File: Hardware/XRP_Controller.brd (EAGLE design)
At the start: 63.5 x 54 mm, 212 parts, among them J1 POWER_JACKPOWER_JACK_SLOT, J12 Vertical Qwiic Connector, J13 Vertical Qwiic Connector, J14 Vertical Qwiic Connector, J3 JST_6_PIN_VERTICAL, J4 JST_6_PIN_VERTICAL, J5 JST_6_PIN_VERTICAL, J6 JST_6_PIN_VERTICAL, J9 Vertical Qwiic Connector, Q3 20V/4.2A/52mΩ/1.4W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

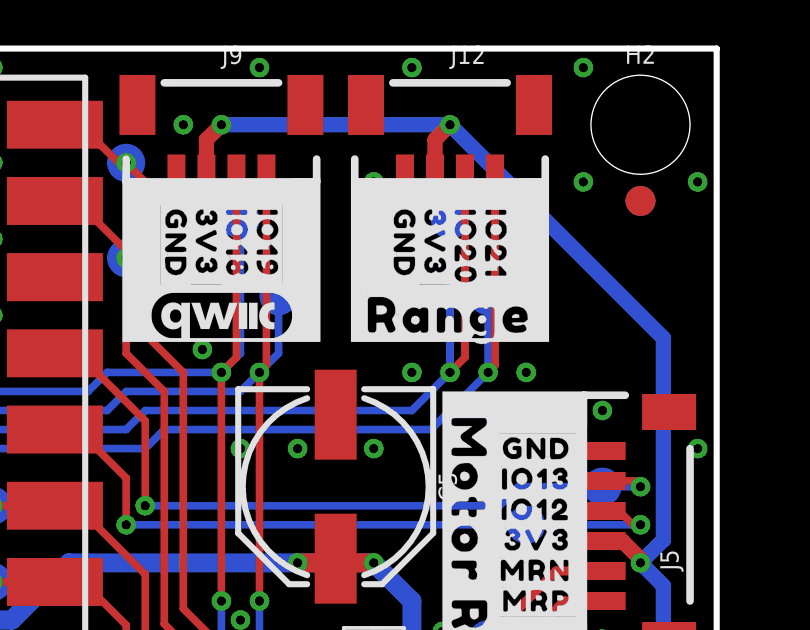
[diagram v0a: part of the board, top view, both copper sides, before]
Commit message: Fix "Range" silk
Modify the Buzzard footprint to have a lower bottom edge
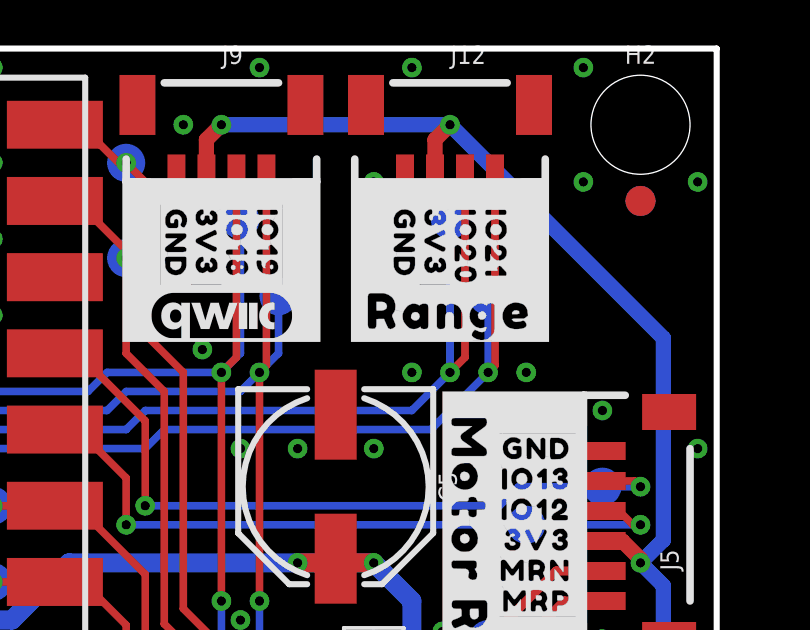
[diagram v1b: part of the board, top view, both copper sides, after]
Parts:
- removed U$73: (no value), output:#RANGE#0
- added U$69: (no value), output:#RANGE#0
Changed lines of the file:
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@@
 <rectangle x1="51.308" y1="44.323" x2="51.435" y2="45.847" layer="21"/>
 <rectangle x1="57.785" y1="44.323" x2="57.912" y2="45.847" layer="21"/>
-<rectangle x1="51.308" y1="44.196" x2="57.912" y2="44.323" layer="21"/>
+<rectangle x1="51.308" y1="44.196" x2="55.372" y2="44.323" layer="21"/>
 <rectangle x1="10.922" y1="45.847" x2="12.192" y2="49.657" layer="21"/>
 <rectangle x1="5.588" y1="45.847" x2="6.858" y2="49.657" layer="21"/>
@@
 <rectangle x1="39.243" y1="31.623" x2="39.624" y2="31.877" layer="41"/>
 <rectangle x1="17.653" y1="16.129" x2="17.907" y2="16.256" layer="41"/>
+<rectangle x1="56.007" y1="44.196" x2="57.912" y2="44.323" layer="21"/>
+<rectangle x1="55.372" y1="44.196" x2="56.007" y2="44.2468" layer="21"/>
 </plain>
 <attributes>
@@
 <attribute name="VALUE" x="17.315" y="19.525" size="1.27" layer="27"/>
 </element>
-<element name="U$73" library="output" package="#RANGE#0" value="" x="54.61" y="45.085" smashed="yes"/>
 <element name="U$74" library="output" package="#LINE#0" value="" x="8.89" y="45.085" smashed="yes"/>
 <element name="U$10" library="output" package="#MOTOR_L#0" value="" x="8.255" y="38.1" smashed="yes" rot="R90"/>
@@
 <element name="TP39" library="SparkFun-Connectors" package="PAD.03X.05" value="TEST-POINT3X5" x="50.8" y="22.86" smashed="yes" rot="MR0"/>
 <element name="TP38" library="SparkFun-Connectors" package="PAD.03X.05" value="TEST-POINT3X5" x="45.085" y="19.685" smashed="yes" rot="MR0"/>
+<element name="U$69" library="output" package="#RANGE#0" value="" x="54.61" y="45.212" smashed="yes"/>
 </elements>
 <signals>

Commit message: Connect SCX pin of IMU to GND
Datasheet says to do this, whoops!
Pins 10-12 have internal pullups, can leave unconnected
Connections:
- net GND: now also U4.3
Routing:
- net GND: track 7.35 -> 8.08 mm
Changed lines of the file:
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@@
 <via x="7.239" y="26.289" extent="1-16" drill="0.3048"/>
 <wire x1="45.815" y1="23.11" x2="45.3106625" y2="23.11" width="0.254" layer="1"/>
-<wire x1="45.085" y1="22.8843375" x2="45.085" y2="22.225" width="0.254" layer="1"/>
+<wire x1="45.085" y1="22.8843375" x2="45.085" y2="22.606" width="0.254" layer="1"/>
+<wire x1="45.085" y1="22.606" x2="45.085" y2="22.225" width="0.254" layer="1"/>
 <wire x1="45.3106625" y1="23.11" x2="45.085" y2="22.8843375" width="0.254" layer="1"/>
 <contactref element="J8" pad="3"/>
@@
 <contactref element="U1" pad="28"/>
 <via x="50.8" y="21.336" extent="1-16" drill="0.3048"/>
+<contactref element="U4" pad="3"/>
+<wire x1="45.815" y1="22.61" x2="45.089" y2="22.61" width="0.254" layer="1"/>
+<wire x1="45.089" y1="22.61" x2="45.085" y2="22.606" width="0.254" layer="1"/>
 </signal>
 <signal name="3.3V">

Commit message: Put all XRP specific parts into a single library
Helps ensure PROD_ID values are correct for this project
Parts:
- U1: value RPI_PICO_W -> RPI_PICO_W_XRP; device RPI_PICO_W:RPI_PICO_W -> XRP_COMPONENTS:RPI_PICO_W
- U4: value LSM6DS0 -> LSM6DS0X; device SparkFun-Sensors:LGA14L -> XRP_COMPONENTS:LGA14L
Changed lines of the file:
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@@
 <attribute name="VALUE" x="47.006" y="51.40866875" size="0.6096" layer="27"/>
 </element>
-<element name="U4" library="SparkFun-Sensors" package="LGA14L" value="LSM6DS0" x="46.99" y="22.86" smashed="yes">
+<element name="U4" library="XRP_COMPONENTS" package="LGA14L" value="LSM6DS0X" x="46.99" y="22.86" smashed="yes">
 <attribute name="NAME" x="45.633" y="24.632" size="0.6096" layer="27" font="vector" ratio="20"/>
-<attribute name="PROD_ID" value="IC-15837" x="46.99" y="22.86" size="1.778" layer="27" font="vector" ratio="15" display="off"/>
-<attribute name="VALUE" x="45.379" y="20.469" size="0.6096" layer="27" font="vector" ratio="20"/>
+<attribute name="PROD_ID" value="IC-18009" x="46.99" y="22.86" size="1.778" layer="27" font="vector" ratio="15" display="off"/>
+<attribute name="VALUE" value="LSM6DS0X" x="45.379" y="20.469" size="0.6096" layer="27" font="vector" ratio="20"/>
 </element>
 <element name="U5" library="SparkFun-IC-Special-Function" package="WSON-12" value="DRV8835" x="11.43" y="33.02" smashed="yes" rot="R270">
@@
 <attribute name="VALUE" x="9.144" y="16.129" size="0.6096" layer="27" font="vector" ratio="20" rot="R90" align="top-center"/>
 </element>
-<element name="U1" library="RPI_PICO_W" package="RPI_PICO_W" value="RPI_PICO_W" x="31.75" y="27.305" smashed="yes" rot="R180">
+<element name="U1" library="XRP_COMPONENTS" package="RPI_PICO_W" value="RPI_PICO_W_XRP" x="31.75" y="27.305" smashed="yes" rot="R180">
 <attribute name="NAME" x="31.75" y="-0.195" size="0.6096" layer="25" font="vector" ratio="20" rot="R180" align="center"/>
-<attribute name="PROD_ID" value="COMP-16830" x="31.75" y="27.305" size="1.778" layer="27" font="vector" ratio="15" rot="R180" display="off"/>
+<attribute name="PROD_ID" value="COMP-18042" x="31.75" y="27.305" size="1.778" layer="27" font="vector" ratio="15" rot="R180" display="off"/>
 <attribute name="VALUE" x="31.75" y="54.805" size="0.6096" layer="27" font="vector" ratio="20" rot="R180" align="center"/>
 </element>

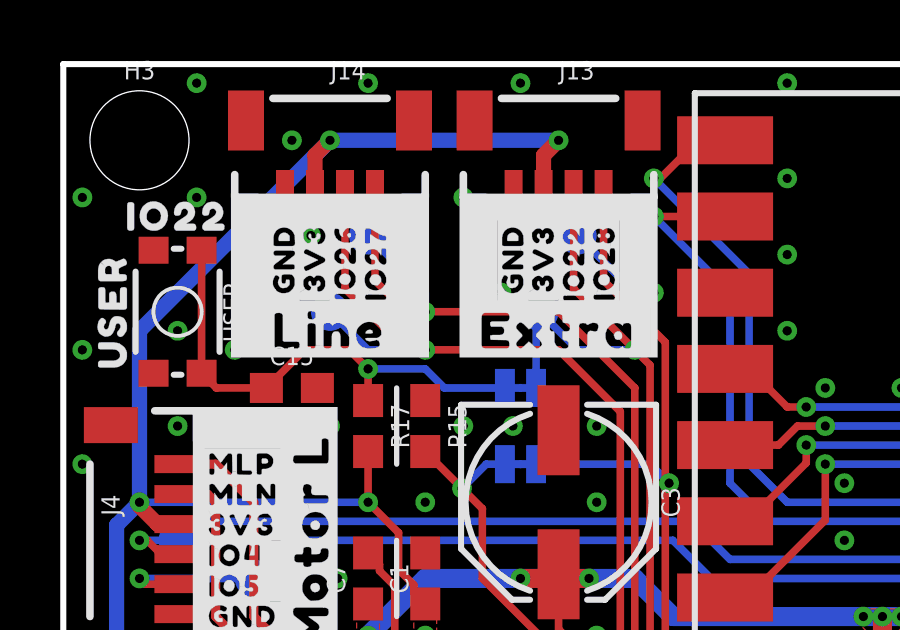
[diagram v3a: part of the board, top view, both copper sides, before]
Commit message: Nudge vias to clean up silk text
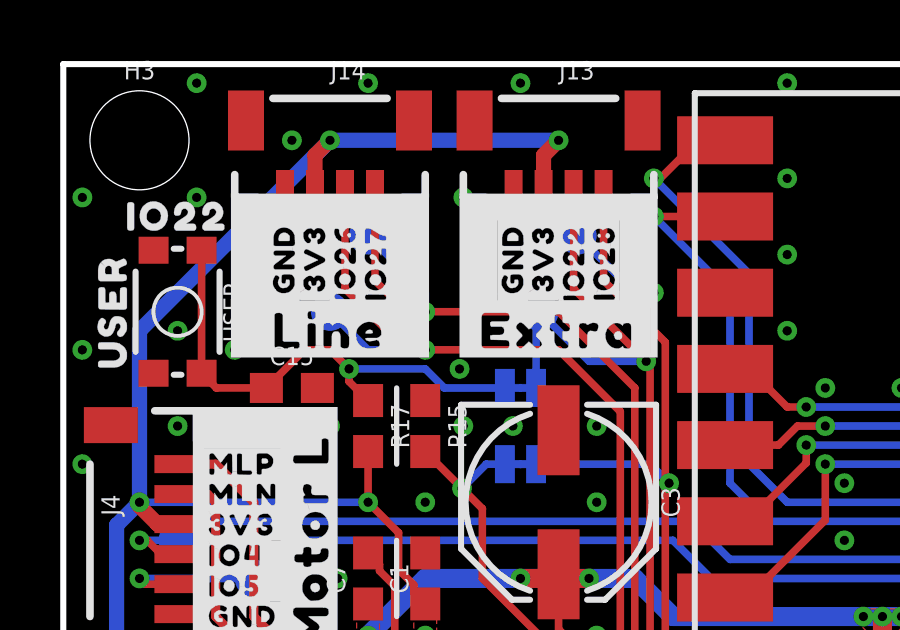
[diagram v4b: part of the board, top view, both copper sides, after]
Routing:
- net RP_IO22/USER_BTN: track 28.2 -> 28.7 mm
- net GND: vias 202 -> 203
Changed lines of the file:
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@@
 <via x="38.735" y="8.89" extent="1-16" drill="0.3048"/>
 <via x="59.69" y="12.7" extent="1-16" drill="0.3048"/>
-<via x="14.605" y="46.355" extent="1-16" drill="0.3048"/>
-<via x="8.255" y="48.26" extent="1-16" drill="0.3048"/>
+<via x="13.97" y="46.355" extent="1-16" drill="0.3048"/>
+<via x="6.35" y="47.625" extent="1-16" drill="0.3048"/>
 <contactref element="R15" pad="1"/>
 <via x="13.335" y="41.91" extent="1-16" drill="0.3048"/>
@@
 <wire x1="45.815" y1="22.61" x2="45.089" y2="22.61" width="0.254" layer="1"/>
 <wire x1="45.089" y1="22.61" x2="45.085" y2="22.606" width="0.254" layer="1"/>
+<via x="13.208" y="43.815" extent="1-16" drill="0.3048"/>
 </signal>
 <signal name="3.3V">
@@
 <wire x1="19.558" y1="31.496" x2="19.558" y2="43.942" width="0.254" layer="1"/>
 <contactref element="J13" pad="3"/>
-<wire x1="19.558" y1="43.942" x2="19.05" y2="44.45" width="0.254" layer="1"/>
+<wire x1="19.558" y1="43.942" x2="19.431" y2="44.069" width="0.254" layer="1"/>
 <contactref element="TP21" pad="1"/>
-<via x="19.05" y="44.45" extent="1-16" drill="0.3048"/>
-<wire x1="19.05" y1="44.45" x2="17.145" y2="44.45" width="0.254" layer="16"/>
-<wire x1="17.145" y1="44.45" x2="15.875" y2="45.72" width="0.254" layer="16"/>
+<via x="19.431" y="44.069" extent="1-16" drill="0.3048"/>
+<wire x1="19.431" y1="44.069" x2="17.526" y2="44.069" width="0.254" layer="16"/>
+<wire x1="17.526" y1="44.069" x2="15.875" y2="45.72" width="0.254" layer="16"/>
 <contactref element="USER_BTN" pad="2"/>
 <wire x1="15.7607" y1="43.18" x2="15.7607" y2="45.6057" width="0.254" layer="16"/>
 <wire x1="15.7607" y1="45.6057" x2="15.875" y2="45.72" width="0.254" layer="16"/>
 <wire x1="17.01" y1="49.67" x2="17.01" y2="46.49" width="0.254" layer="1"/>
-<wire x1="17.01" y1="46.49" x2="19.05" y2="44.45" width="0.254" layer="1"/>
+<wire x1="17.01" y1="46.49" x2="19.431" y2="44.069" width="0.254" layer="1"/>
 <contactref element="U1" pad="29"/>
 </signal>
@@
 <wire x1="4.61" y1="43.67" x2="5.1" y2="43.18" width="0.254" layer="1"/>
 <wire x1="5.1" y1="43.18" x2="6.77" y2="43.18" width="0.254" layer="1"/>
-<wire x1="10.16" y1="42.76" x2="10.16" y2="43.815" width="0.254" layer="1"/>
-<wire x1="10.16" y1="43.815" x2="9.525" y2="44.45" width="0.254" layer="1"/>
-<wire x1="9.525" y1="44.45" x2="8.04" y2="44.45" width="0.254" layer="1"/>
+<wire x1="10.16" y1="42.76" x2="9.525" y2="43.395" width="0.254" layer="1"/>
+<wire x1="9.525" y1="43.815" x2="9.525" y2="43.395" width="0.254" layer="1"/>
+<wire x1="9.525" y1="43.815" x2="8.89" y2="44.45" width="0.254" layer="1"/>
+<wire x1="8.89" y1="44.45" x2="8.04" y2="44.45" width="0.254" layer="1"/>
 <wire x1="8.04" y1="44.45" x2="6.77" y2="43.18" width="0.254" layer="1"/>
-<via x="10.16" y="43.815" extent="1-16" drill="0.3048"/>
-<wire x1="10.16" y1="43.815" x2="12.065" y2="43.815" width="0.254" layer="16"/>
+<via x="9.525" y="43.815" extent="1-16" drill="0.3048"/>
+<wire x1="9.525" y1="43.815" x2="12.065" y2="43.815" width="0.254" layer="16"/>
 <wire x1="12.065" y1="43.815" x2="12.7" y2="43.18" width="0.254" layer="16"/>
 <wire x1="12.7" y1="43.18" x2="14.7193" y2="43.18" width="0.254" layer="16"/>

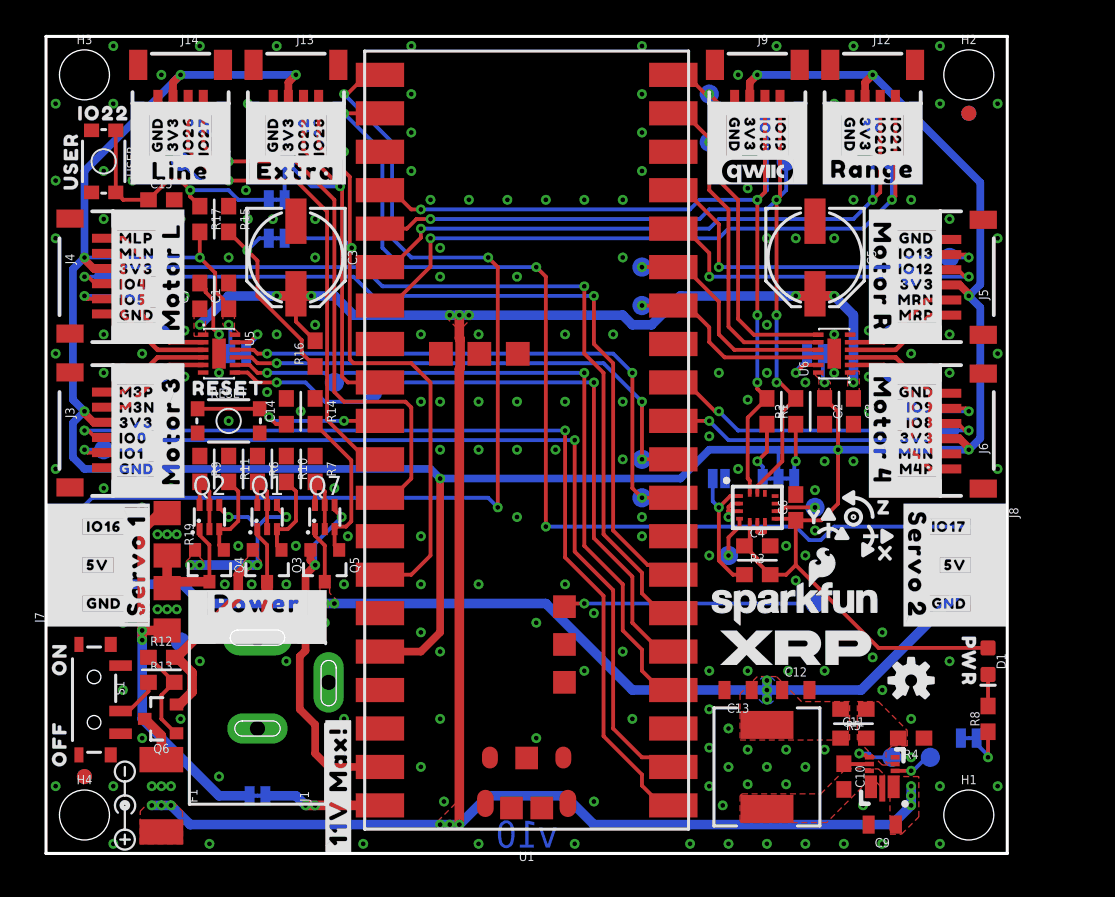
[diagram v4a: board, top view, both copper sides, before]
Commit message: Minor tweaks
Nudge I2C jumper back onto grid
Nudge a couple power traces under Pico W
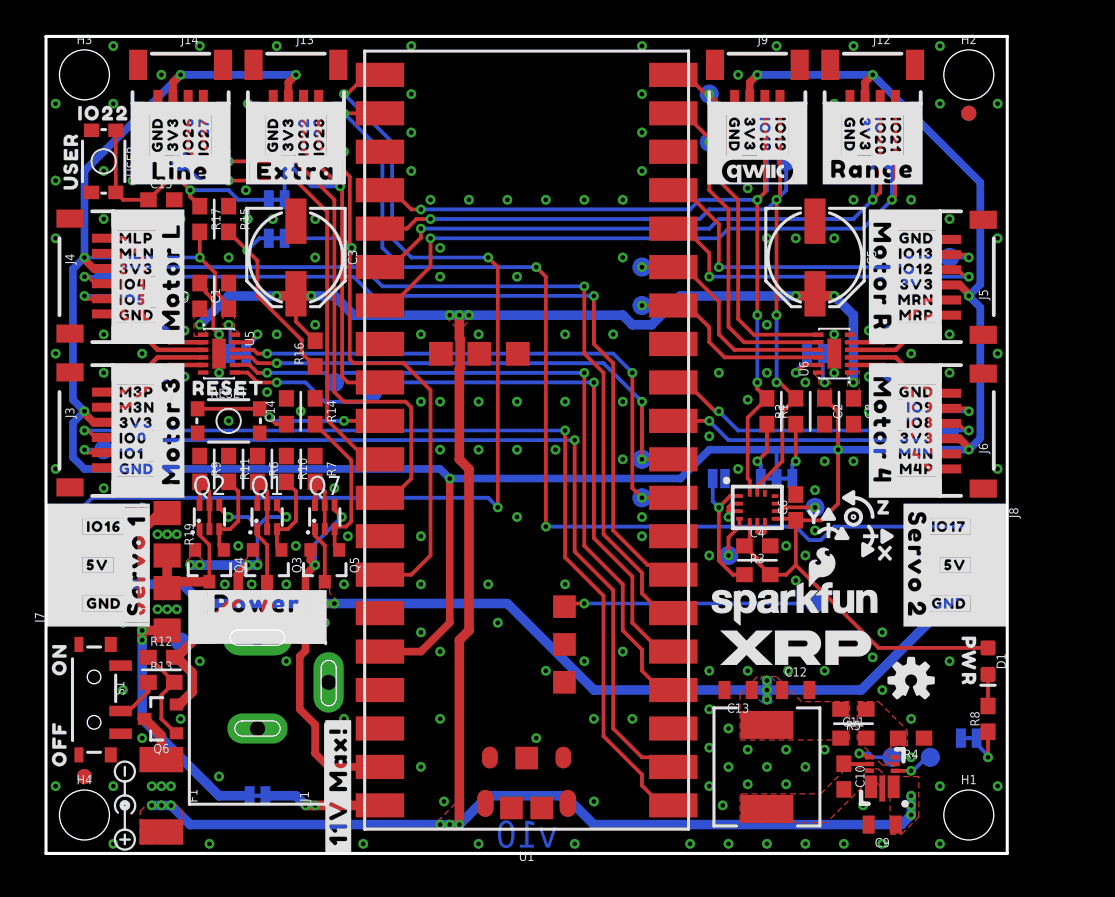
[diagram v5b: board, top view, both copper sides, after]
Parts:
- moved I2C 0.13 mm to (48.3, 24.8)
- moved U$60 0.13 mm to (49.5, 24.8)
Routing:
- net GND: vias 203 -> 204

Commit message: Design review updates
Motor mode jumpers - add "/3" and "/4" to jumper names
Overlay copper version number with silk version number
Change IMU_ADR jumper from NO to NC, and swap with R3 to keep same default address
Add second power LED to indicate motor power vs system power
Change power LEDs to DIO-17976 and corresponding resistor values
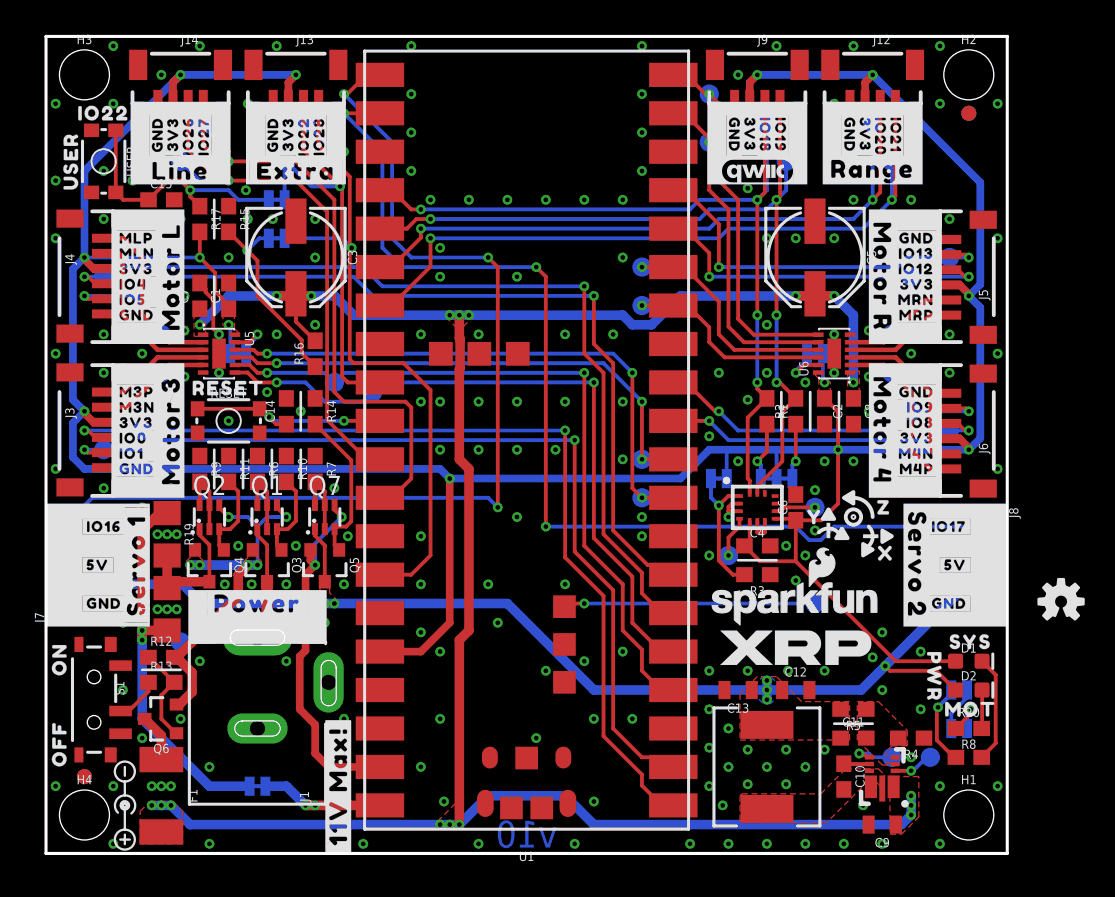
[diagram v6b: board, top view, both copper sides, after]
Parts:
- removed PWR: JUMPER-SMT_2_NC_TRACE_SILK, SparkFun-Jumpers:SMT-JUMPER_2_NC_TRACE_SILK
- removed U$94: (no value), output:#PWR#0
- added D2: Red, SparkFun-LED:LED-0603
- added MOT_PWR, SYS_PWR: JUMPER-SMT_2_NC_TRACE_SILK, SparkFun-Jumpers:SMT-JUMPER_2_NC_TRACE_SILK
- added R20: 10k, SparkFun-Resistors:0603
- added U$70: (no value), output:#MOT_MODE_R#4#0
- added U$71: (no value), output:MOT0
- added U$73: (no value), output:#PWR#0
- added U$95: (no value), output:#MOT#0
- added U$96: (no value), output:#SYS#0
- IMU_ADR: value JUMPER-SMT_2_NO_SILK -> JUMPER-SMT_2_NC_TRACE_SILK; device SparkFun-Jumpers:SMT-JUMPER_2_NO_SILK -> SparkFun-Jumpers:SMT-JUMPER_2_NC_TRACE_SILK
- R8: value 1k -> 4.7k
- U$66: device output:#MOT_MODE_R#0 -> output:#MOT_MODE_L#3#0
- U$67: device output:#MOT_MODE_L#0 -> output:SYS0
- moved U$67 51.2 mm to (61.1, 14.0), flipped to the top
- moved U$66 36.4 mm to (13.5, 33.0)
- moved LOGO1 11.2 mm to (67.1, 16.6)
- moved R8 2.84 mm to (61.0, 6.35), turned to 0 degrees
- moved U$6 2.50 mm to (58.7, 11.7)
- moved U$87 1.27 mm to (38.6, 21.1)
- moved U$91 1.27 mm to (38.6, 22.4)
- moved D1 1.27 mm to (61.0, 12.7), turned to 0 degrees
- moved U$93 0.64 mm to (14.7, 4.45)
- moved VUSB 0.64 mm to (14.0, 4.45)
- moved U$64 0.13 mm to (43.6, 24.8)
- turned IMU_ADR to 180 degrees
- turned R3 to 180 degrees
- renumbered MOT_MODE_L to MOT_MODE_L/3, MOT_MODE_R to MOT_MODE_R/4
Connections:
- new net N$21: D2.C, R20.2
- new net N$22: MOT_PWR.2, R20.1
- net 3.3V: now also IMU_ADR.2; no longer R3.2
- net 5V: now also D2.A
- net GND: now also MOT_PWR.1, R3.1, SYS_PWR.1; no longer IMU_ADR.1, PWR.1
- net N$10: now also SYS_PWR.2; no longer PWR.2
- net N$2: now also IMU_ADR.1, R3.2; no longer IMU_ADR.2, R3.1
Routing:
- net 5V: track 72.6 -> 77.9 mm, vias 5 -> 6
- net N$1: track 2.08 -> 7.11 mm
- net N$22: track 0.00 -> 3.04 mm, vias 0 -> 1
- net GND: track 8.08 -> 11.1 mm
- net N$21: track 0.00 -> 2.55 mm
- net N$10: track 3.27 -> 5.44 mm
- net 3.3V: track 218.2 -> 217.4 mm
